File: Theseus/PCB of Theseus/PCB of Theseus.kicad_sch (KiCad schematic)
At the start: 25 parts, among them J3 G125-MH104M4-04AD000P, J7 4DB-P108-02, U1 TPS565201DDC, U3 TCAN334

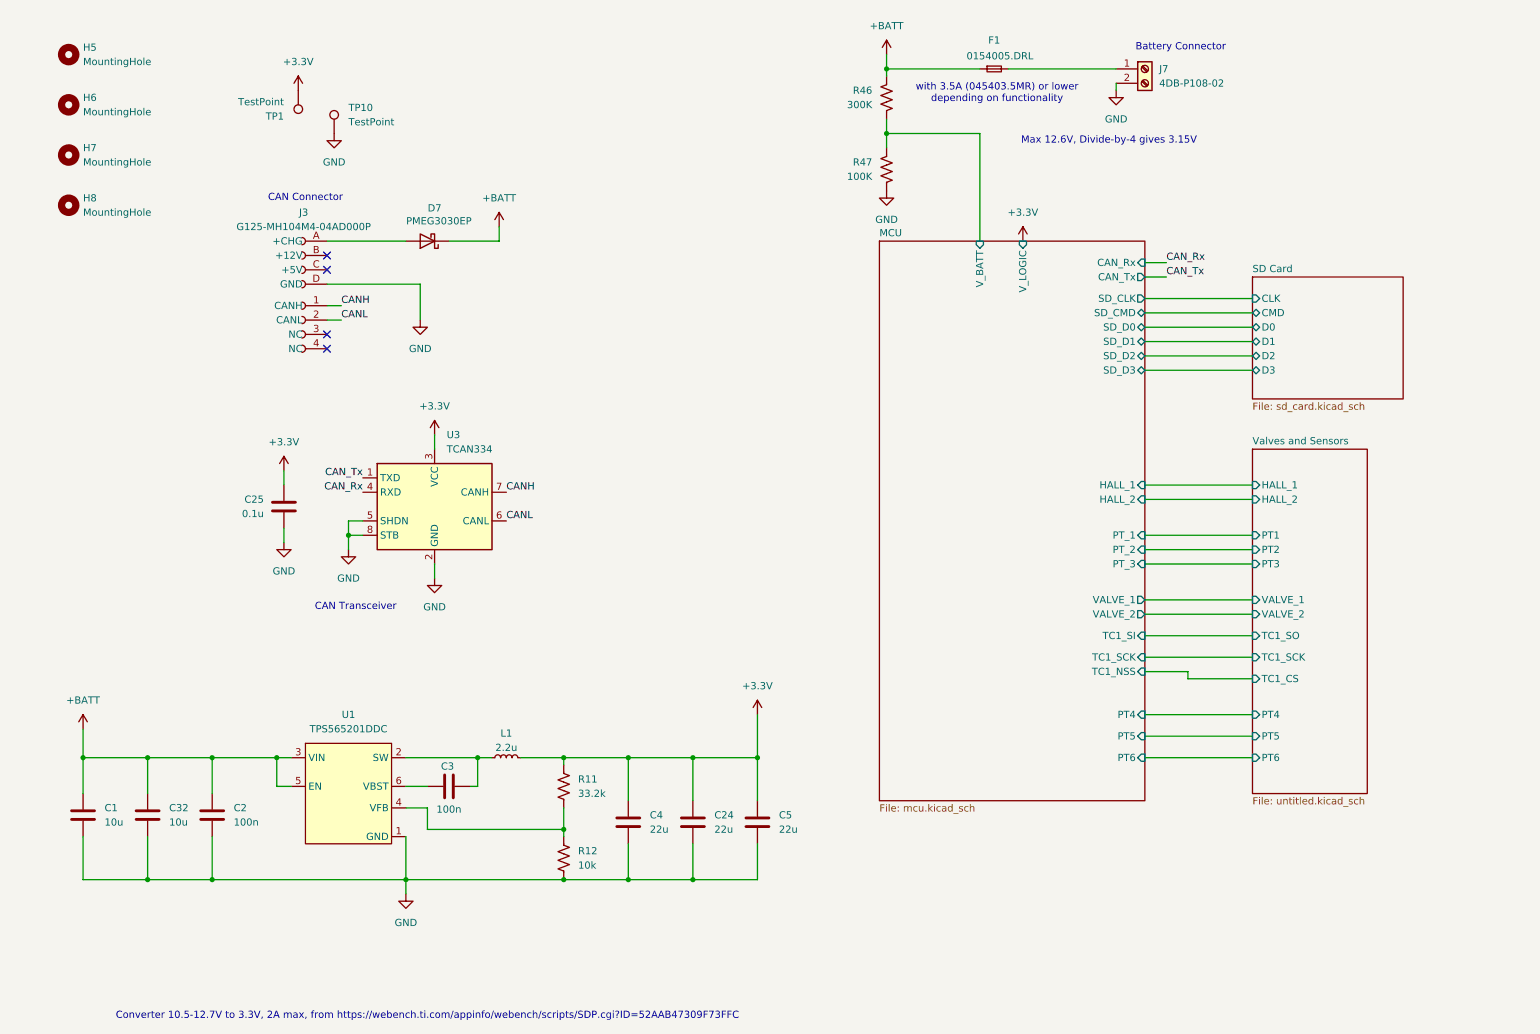
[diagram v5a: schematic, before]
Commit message: layout and routing + minor schematic changes
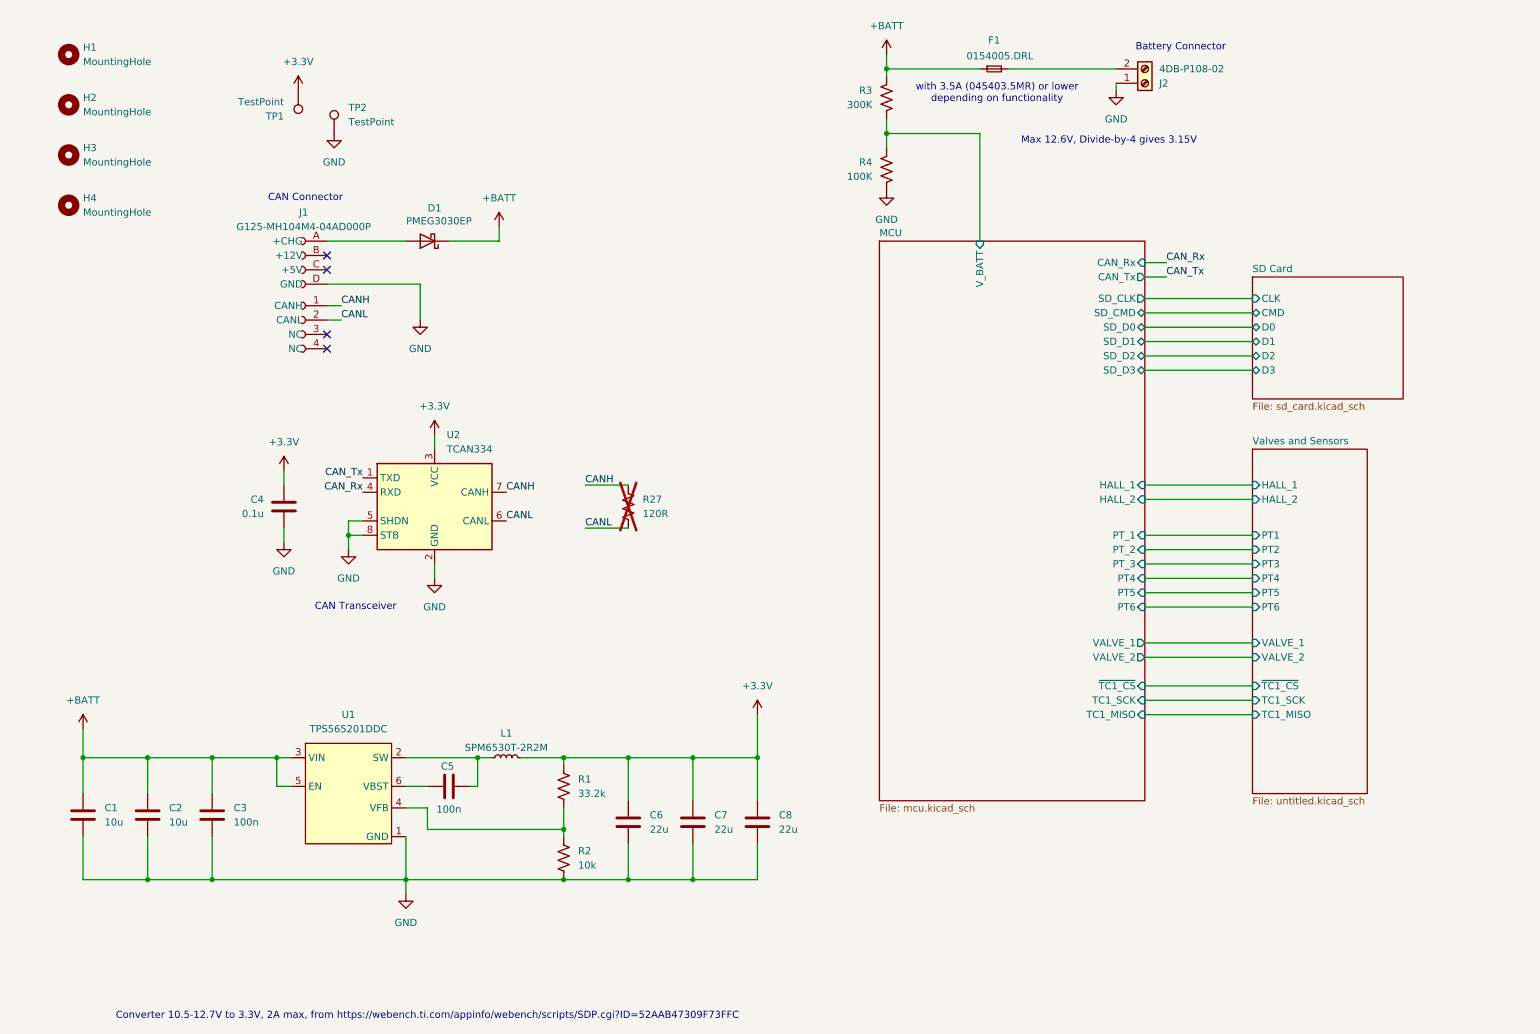
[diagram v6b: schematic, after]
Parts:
- added R27: 120R, Resistor_SMD:R_0603_1608Metric_Pad0.98x0.95mm_HandSolder, symbol Device:R_US
- H1: renamed from H5; footprint MountingHole:MountingHole_4.3mm_M4 -> MountingHole:MountingHole_3.2mm_M3_ISO14580
- H2: renamed from H6; footprint MountingHole:MountingHole_4.3mm_M4 -> MountingHole:MountingHole_3.2mm_M3_ISO14580
- H3: renamed from H7; footprint MountingHole:MountingHole_4.3mm_M4 -> MountingHole:MountingHole_3.2mm_M3_ISO14580
- H4: renamed from H8; footprint MountingHole:MountingHole_4.3mm_M4 -> MountingHole:MountingHole_3.2mm_M3_ISO14580
- L1: value 2.2u -> SPM6530T-2R2M; footprint Fydp_footprints:SPM6530T-2R2M -> Fydp_footprints:IND_SPM6530T-2R2M
- renumbered C32 to C2, C2 to C3, C25 to C4, C3 to C5, C4 to C6, C24 to C7, C5 to C8, D7 to D1, J3 to J1, J7 to J2, R11 to R1, R12 to R2, R46 to R3, R47 to R4, TP10 to TP2, U3 to U2
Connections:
- net CANH: now also R27.1
- net CANL: now also R27.2
- net GND: now also J2.1 (Pin_1); no longer J2.2 (Pin_2)
- net at F1.2: now also J2.2 (Pin_2); no longer J2.1 (Pin_1)
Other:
- sheet MCU ports: added TC1_MISO, ~{TC1_CS}; removed TC1_NSS, TC1_SI, V_LOGIC
- sheet Valves and Sensors ports: added TC1_MISO, ~{TC1_CS}; removed TC1_CS, TC1_SO
